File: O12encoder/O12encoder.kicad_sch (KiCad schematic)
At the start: 15 parts, among them J1 Conn_01x06_Pin, J2 Conn_01x06_Pin, J3 Conn_01x06_Pin, J4 Conn_01x06_Pin, J5 JST_SM02B-SRSS-TB(LF)(SN), J6 JST_SM02B-SRSS-TB(LF)(SN), U1 MA702GQ-P, U2 STM32L011F4Ux, U3 THVD1420DRLR

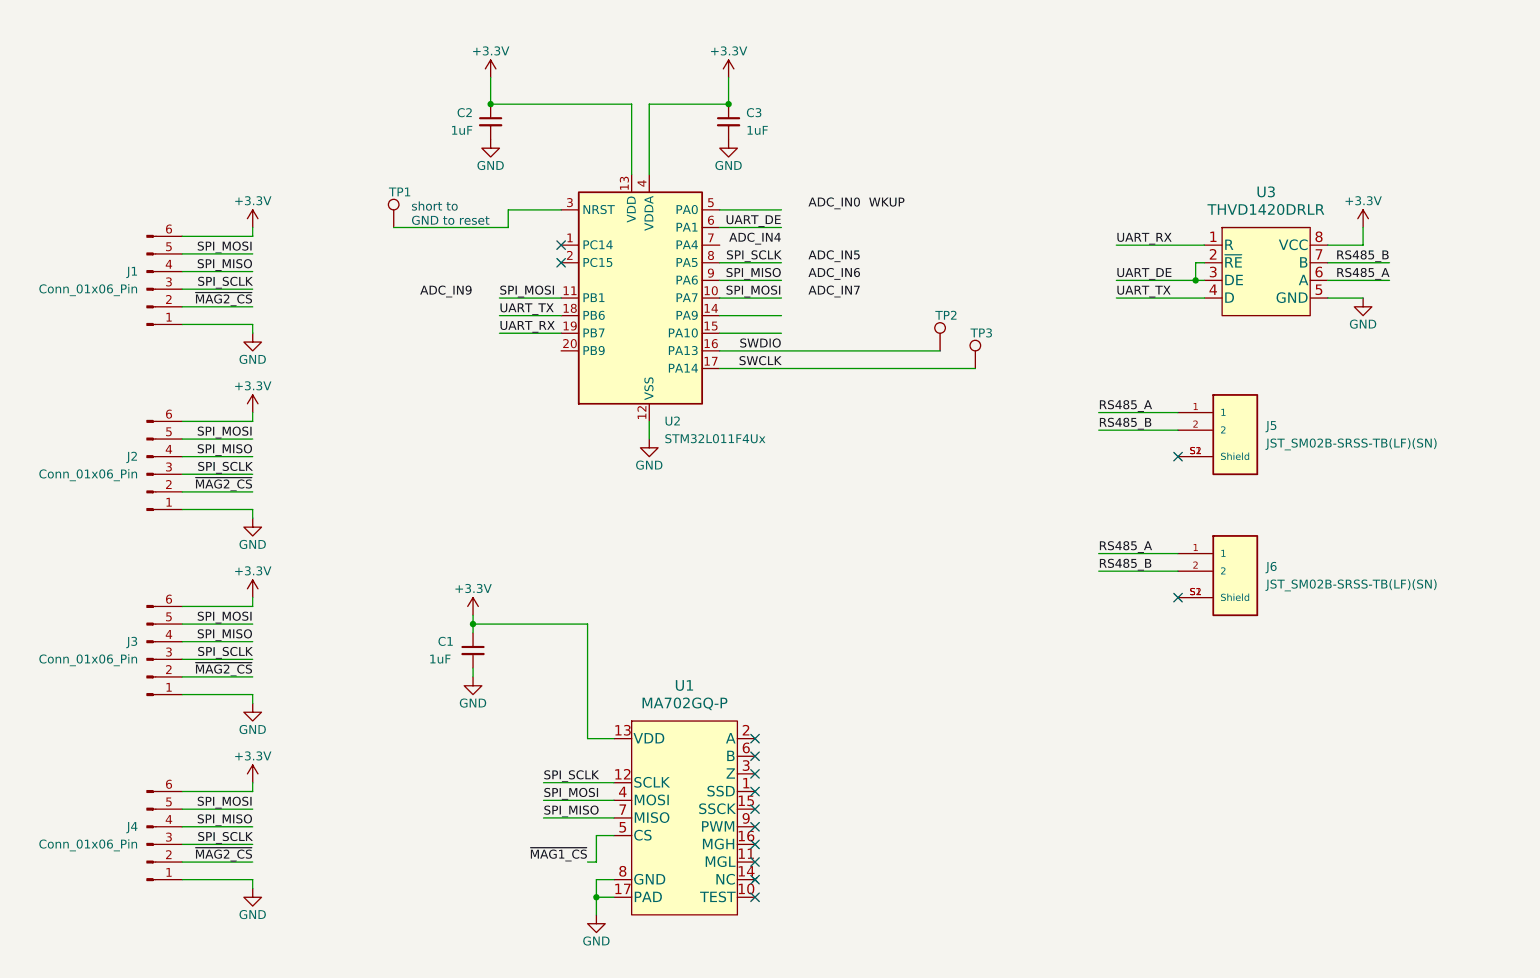
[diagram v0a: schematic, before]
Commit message: encoder change to both sides FFC
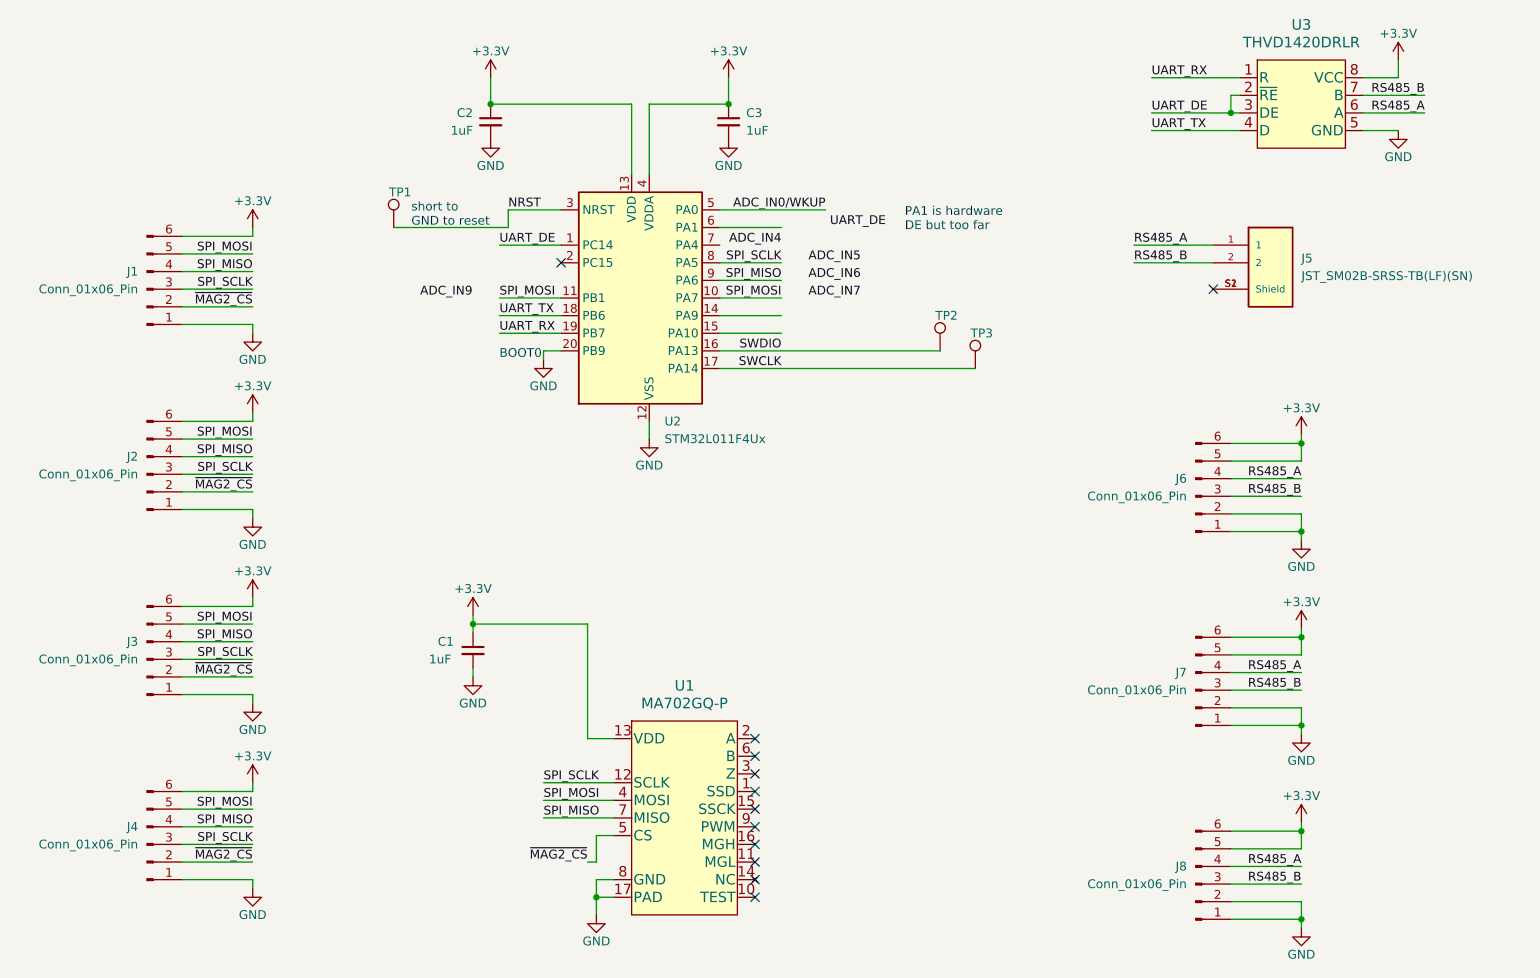
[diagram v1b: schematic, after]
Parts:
- removed J6: JST_SM02B-SRSS-TB(LF)(SN), O32controller:JST_SM02B-SRSS-TB(LF)(SN), symbol O32controller:JST_SM02B-SRSS-TB(LF)(SN)
- added J6, J7, J8: Conn_01x06_Pin, O32controller:FFC_0.5mm_6p, symbol Connector:Conn_01x06_Pin
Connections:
- net ~{MAG1_CS} is gone; now on net ~{MAG2_CS}: U1.5 (CS)
- net +3.3V: now also J6.5 (Pin_5), J6.6 (Pin_6), J7.5 (Pin_5), J7.6 (Pin_6), J8.5 (Pin_5), J8.6 (Pin_6)
- net GND: now also U2.20 (PB9), J6.1 (Pin_1), J6.2 (Pin_2), J7.1 (Pin_1), J7.2 (Pin_2), J8.1 (Pin_1), J8.2 (Pin_2)
- net RS485_A: now also J6.4 (Pin_4), J7.4 (Pin_4), J8.4 (Pin_4)
- net RS485_B: now also J6.3 (Pin_3), J7.3 (Pin_3), J8.3 (Pin_3)
- net UART_DE: now also U2.1 (PC14); no longer U2.6 (PA1)
- net NRST: now reaches TP1.1, U2.3 (NRST)
- net ADC_IN0/WKUP: now reaches U2.5 (PA0)
- no-connect marks 14 -> 12
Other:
- note added: "BOOT0"
- note added: "PA1 is hardware DE but too far"
- moved on the sheet: J5, U3

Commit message: undo autoroute
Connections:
- net SPI_MOSI: no longer U2.11 (PB1)
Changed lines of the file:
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@@
     (effects (font (size 1.27 1.27)) (justify right bottom))
   )
-  (label "SPI_MOSI" (at 119.38 64.77 0) (fields_autoplaced)
-    (effects (font (size 1.27 1.27)) (justify left bottom))
+  (label "SPI_MOSI" (at 106.045 65.405 180) (fields_autoplaced)
+    (effects (font (size 1.27 1.27)) (justify right bottom))
   )
   (label "ADC_IN5" (at 171.45 59.69 180) (fields_autoplaced)

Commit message: Revert "encoder change to both sides FFC"
This reverts commit 631d04212b57ce457fbe4c2d518c1d39f3519578.
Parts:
- removed J6, J7, J8: Conn_01x06_Pin, O32controller:FFC_0.5mm_6p, symbol Connector:Conn_01x06_Pin
- added J6: JST_SM02B-SRSS-TB(LF)(SN), O32controller:JST_SM02B-SRSS-TB(LF)(SN), symbol O32controller:JST_SM02B-SRSS-TB(LF)(SN)
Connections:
- net GND: no longer U2.20 (PB9)
- net RS485_A: now also J6.1
- net RS485_B: now also J6.2
- net UART_DE: now also U2.6 (PA1); no longer U2.1 (PC14)
- net ~{MAG2_CS}: no longer U1.5 (CS)
- net ADC_IN0/WKUP: no longer names the net of U2.5 (PA0)
- net NRST: no longer names the net of TP1.1, U2.3 (NRST)
- new net: J6.S1 (Shield), J6.S2 (Shield)
- new net ~{MAG1_CS}: U1.5 (CS)
- no-connect marks 12 -> 14
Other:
- note removed: "BOOT0"
- note removed: "PA1 is hardware DE but too far"
- moved on the sheet: J5, U3

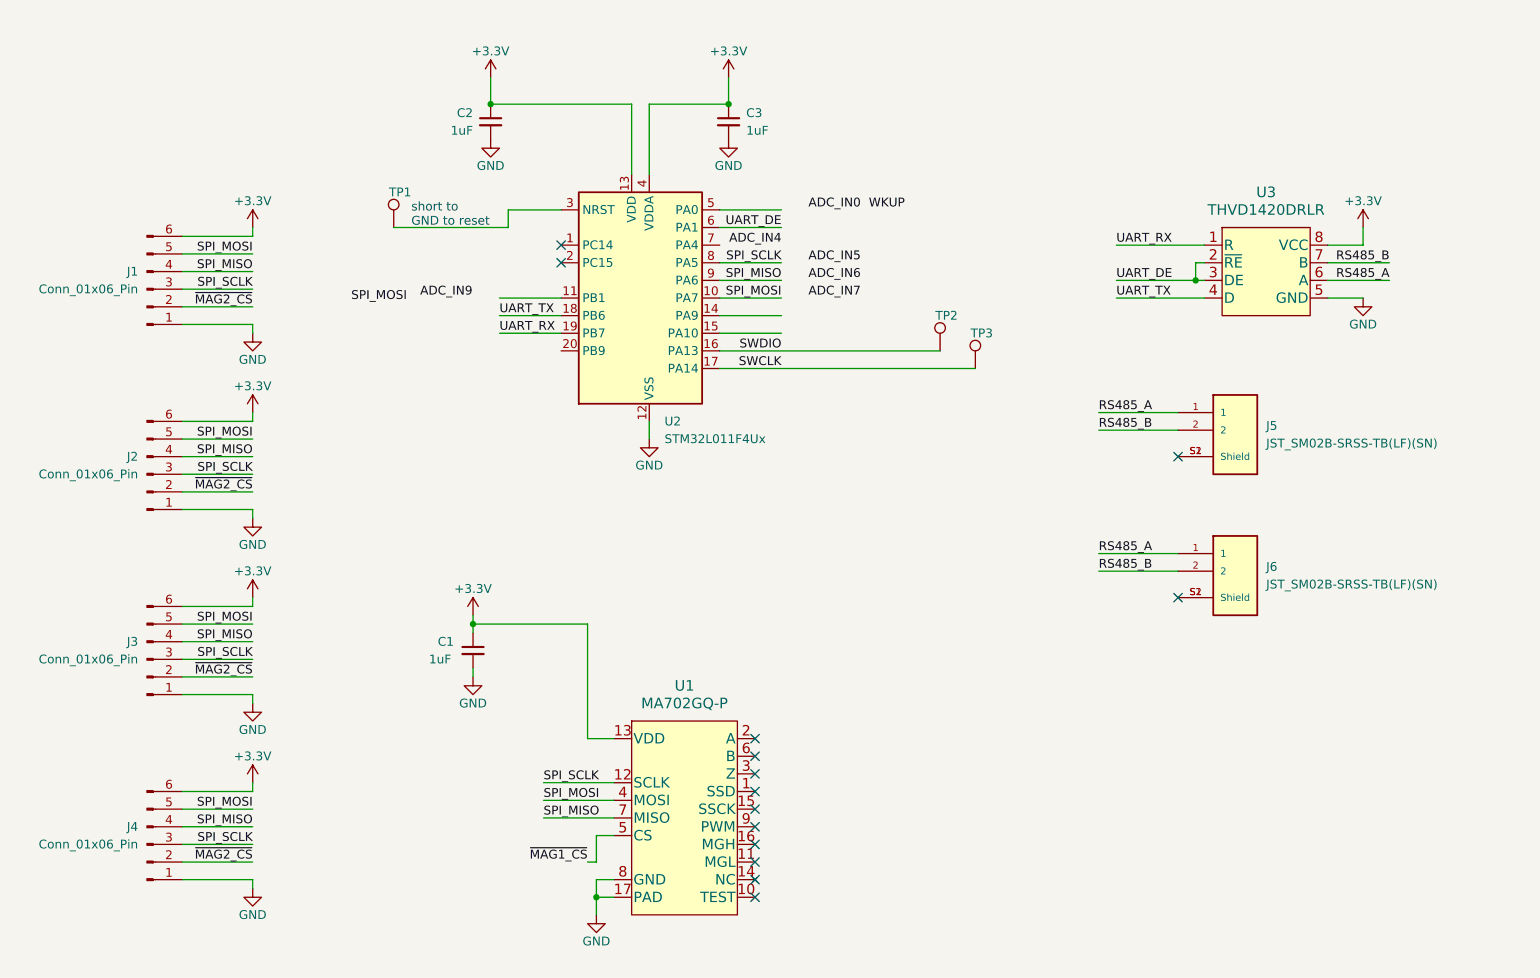
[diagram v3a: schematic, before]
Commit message: routed more, trouble with 3.3 and gnd
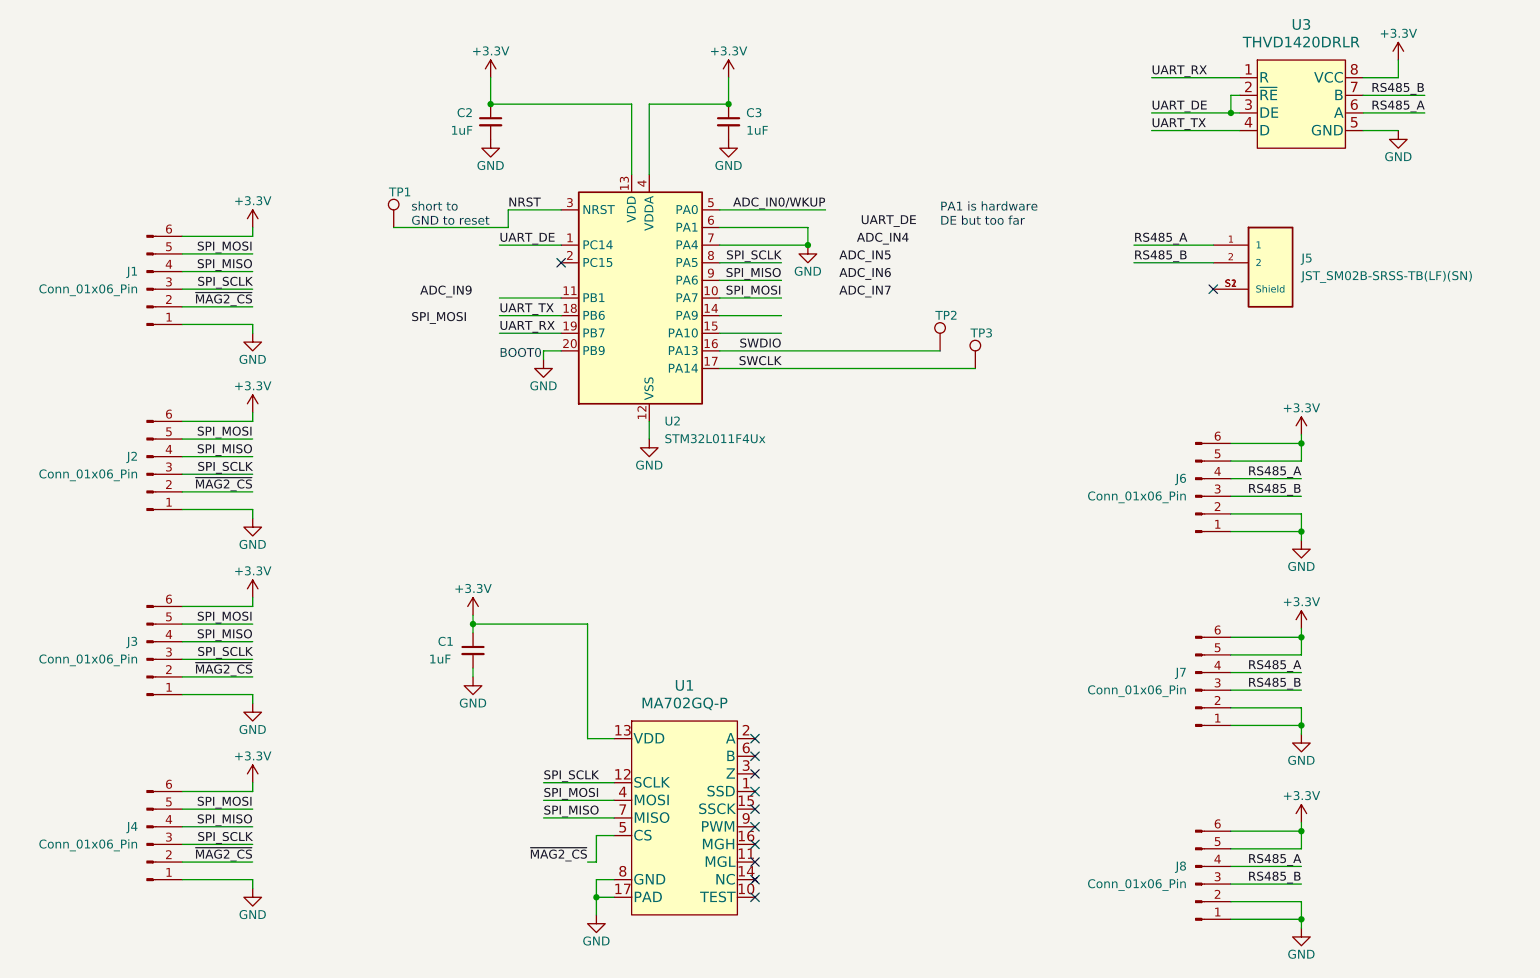
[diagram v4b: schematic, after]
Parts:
- removed J6: JST_SM02B-SRSS-TB(LF)(SN), O32controller:JST_SM02B-SRSS-TB(LF)(SN), symbol O32controller:JST_SM02B-SRSS-TB(LF)(SN)
- added J6, J7, J8: Conn_01x06_Pin, O32controller:FFC_0.5mm_6p, symbol Connector:Conn_01x06_Pin
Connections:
- net ~{MAG1_CS} is gone; now on net ~{MAG2_CS}: U1.5 (CS)
- net +3.3V: now also J6.5 (Pin_5), J6.6 (Pin_6), J7.5 (Pin_5), J7.6 (Pin_6), J8.5 (Pin_5), J8.6 (Pin_6)
- net GND: now also U2.20 (PB9), U2.6 (PA1), U2.7 (PA4), J6.1 (Pin_1), J6.2 (Pin_2), J7.1 (Pin_1), J7.2 (Pin_2), J8.1 (Pin_1), J8.2 (Pin_2)
- net RS485_A: now also J6.4 (Pin_4), J7.4 (Pin_4), J8.4 (Pin_4)
- net RS485_B: now also J6.3 (Pin_3), J7.3 (Pin_3), J8.3 (Pin_3)
- net UART_DE: now also U2.1 (PC14); no longer U2.6 (PA1)
- net NRST: now reaches TP1.1, U2.3 (NRST)
- net ADC_IN0/WKUP: now reaches U2.5 (PA0)
- no-connect marks 14 -> 12
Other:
- note added: "BOOT0"
- note added: "PA1 is hardware DE but too far"
- moved on the sheet: J5, U3

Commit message: done? added silkscreen and pa0 breakout
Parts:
- removed J3: Conn_01x06_Pin, O32controller:FFC_0.5mm_6p, symbol Connector:Conn_01x06_Pin
- added TP4: TestPoint, O32controller:TestPoint_Pad_Rect, symbol Connector:TestPoint
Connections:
- net ADC_IN0/WKUP: now also TP4.1
- net GND: now also U2.2 (PC15); no longer U2.6 (PA1), U2.7 (PA4)
- net RS485_A: now also J5.S1 (Shield), J5.S2 (Shield)
- no-connect marks 12 -> 15
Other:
- note added: "lol"
- note added: "make sure not output"
- moved on the sheet: TP1

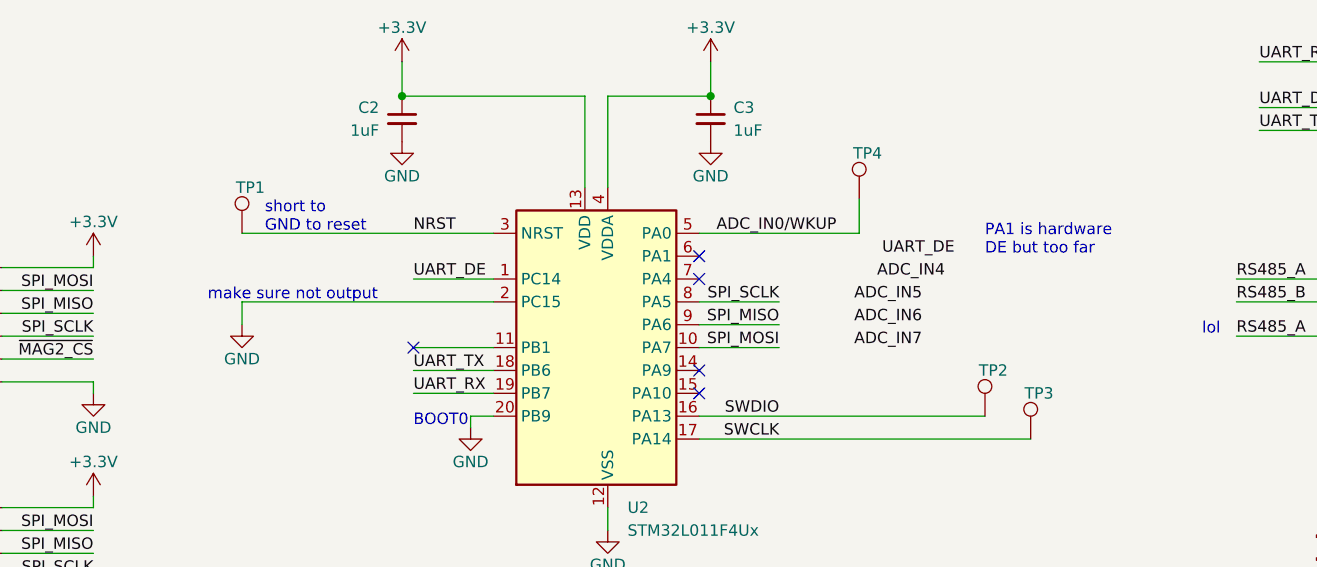
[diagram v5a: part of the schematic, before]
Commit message: clean up schematic
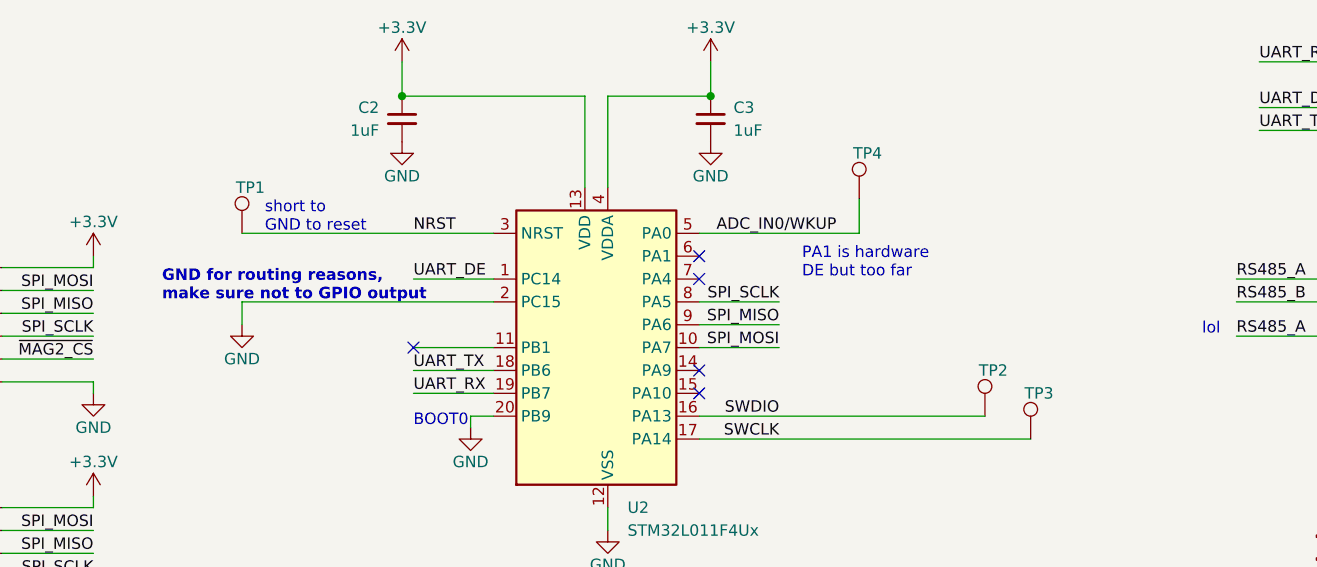
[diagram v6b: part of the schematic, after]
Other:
- note added: "GND for routing reasons, make sure not to GPIO output"
- note removed: "make sure not output"
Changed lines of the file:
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@@
     (stroke (width 0) (type default))
   )
-  (text "make sure not output" (at 96.52 59.69 0)
-    (effects (font (size 1.27 1.27)) (justify left bottom))
+  (text "GND for routing reasons,\nmake sure not to GPIO output"
+    (at 91.44 59.69 0)
+    (effects (font (size 1.27 1.27) (thickness 0.254) bold) (justify left bottom))
   )
   (text "BOOT0" (at 119.38 73.66 0)
     (effects (font (size 1.27 1.27)) (justify left bottom))
   )
-  (text "PA1 is hardware \nDE but too far" (at 182.88 54.61 0)
+  (text "PA1 is hardware \nDE but too far" (at 162.56 57.15 0)
     (effects (font (size 1.27 1.27)) (justify left bottom))
   )
@@
     (effects (font (size 1.27 1.27)) (justify right bottom))
   )
-  (label "ADC_IN7" (at 175.895 64.77 180) (fields_autoplaced)
-    (effects (font (size 1.27 1.27)) (justify right bottom))
-  )
   (label "SPI_MOSI" (at 125.73 137.16 0) (fields_autoplaced)
     (effects (font (size 1.27 1.27)) (justify left bottom))
@@
   )
   (label "RS485_B" (at 234.95 149.225 180) (fields_autoplaced)
-    (effects (font (size 1.27 1.27)) (justify right bottom))
-  )
-  (label "ADC_IN4" (at 178.435 57.15 180) (fields_autoplaced)
     (effects (font (size 1.27 1.27)) (justify right bottom))
   )
@@
     (effects (font (size 1.27 1.27)) (justify right bottom))
   )
-  (label "ADC_IN5" (at 175.895 59.69 180) (fields_autoplaced)
-    (effects (font (size 1.27 1.27)) (justify right bottom))
-  )
   (label "RS485_A" (at 210.82 57.15 0) (fields_autoplaced)
     (effects (font (size 1.27 1.27)) (justify left bottom))
   )
-  (label "UART_DE" (at 171.45 54.61 0) (fields_autoplaced)
-    (effects (font (size 1.27 1.27)) (justify left bottom))
-  )
-  (label "ADC_IN6" (at 175.895 62.23 180) (fields_autoplaced)
-    (effects (font (size 1.27 1.27)) (justify right bottom))
-  )
   (label "~{MAG2_CS}" (at 132.08 146.05 180) (fields_autoplaced)

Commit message: heatsink step, generate Ø12encoder gerbers:
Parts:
- U2: MPN (none) -> STM32L011F4U3TR; Vendor (none) -> Digikey
- U3: MPN (none) -> THVD1420DRLR
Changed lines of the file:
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@@
       (effects (font (size 1.524 1.524)) hide)
+    )
+    (property "MPN" "THVD1420DRLR" (at 234.95 36.83 0)
+      (effects (font (size 1.27 1.27)) hide)
     )
     (pin "1")
@@
       (effects (font (size 1.27 1.27)) hide)
     )
+    (property "MPN" "STM32L011F4U3TR" (at 138.43 64.77 0)
+      (effects (font (size 1.27 1.27)) hide)
+    )
+    (property "Vendor" "Digikey" (at 138.43 64.77 0)
+      (effects (font (size 1.27 1.27)) hide)
+    )
